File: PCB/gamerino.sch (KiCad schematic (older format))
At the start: 47 parts, among them J1 USB_B_Micro, J2 LT2, J3 RT2, P1 JOY1, P2 JOY2, P3 ICSP, P4 AUX, SW1 HATSWITCH, SW10 OPTS, SW11 X, SW12 B, SW13 A, SW14 Y, SW2 LT1, SW3 LT2, SW4 RT1, SW5 RT2, SW6 SEL, SW7 START, SW8 BACK, SW9 HOME, U1 MIC5219-3.3YM5, U2 ATmega32U4, U3 TCA9539, X1 16MHz

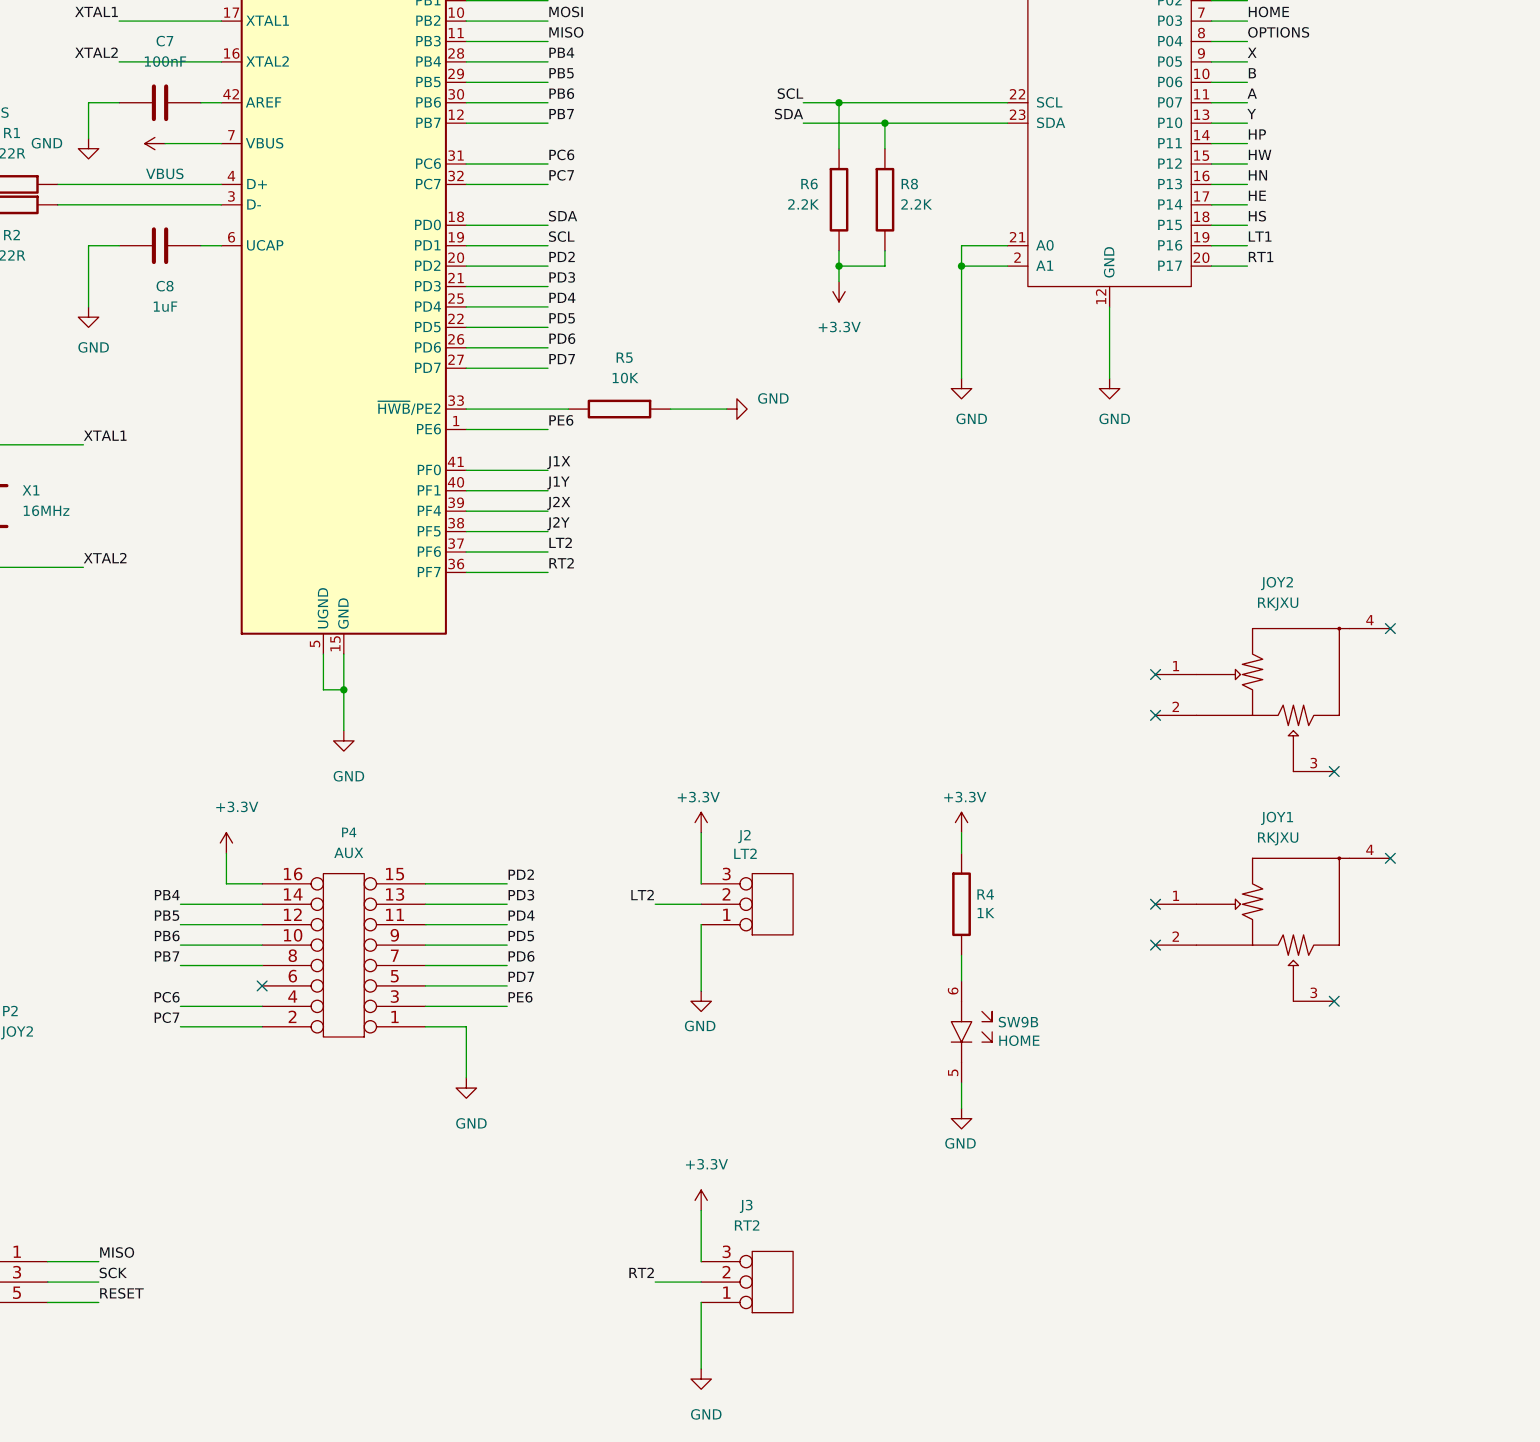
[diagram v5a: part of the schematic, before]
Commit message: Update schematics
Add LHOME net
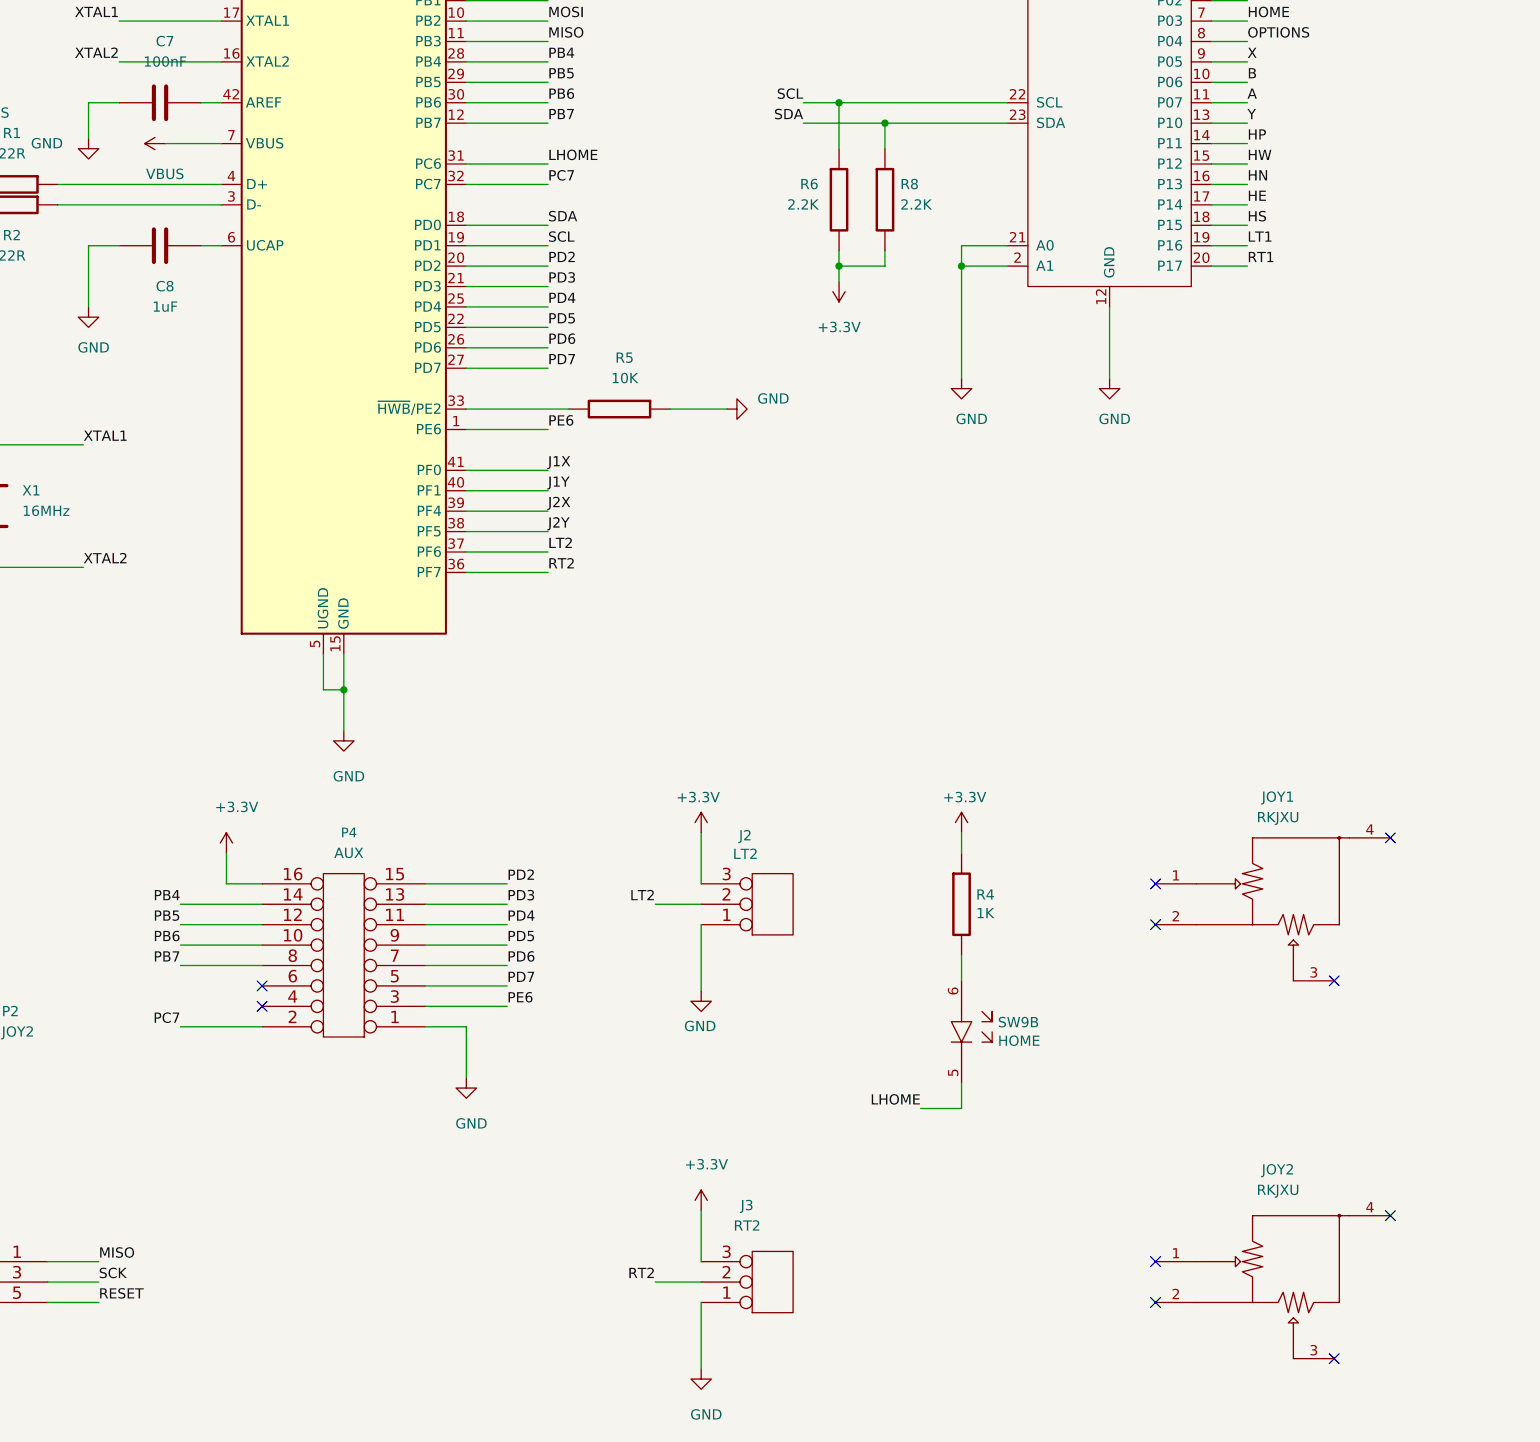
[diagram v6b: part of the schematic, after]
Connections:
- net GND: no longer SW9.5
- net PC6: no longer names the net of P4.4
- net PC6: no longer U2.31 (PC6)
- new net LHOME: SW9.5, U2.31 (PC6)
- no-connect marks 29 -> 30
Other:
- moved on the sheet: JOY1, JOY2
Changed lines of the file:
@@
 	6675 4450 7075 4450
 Text Label 7075 4450 0    50   ~ 0
-PC6
+LHOME
 Wire Wire Line
 	6675 4550 7075 4550
@@
 	1    0    0    -1
 $EndComp
-Wire Wire Line
-	5675 8575 5275 8575
-Text Label 5275 8575 2    50   ~ 0
-PC6
 Wire Wire Line
 	5675 8675 5275 8675
@@
 	9100 8950 9100 9075
 $Comp
-L gamerino-rescue:GND-power #PWR0102
-U 1 1 60BF772D
-P 9100 9075
-F 0 "#PWR0102" H 9100 8825 50  0001 C CNN
-F 1 "GND" H 9105 8902 50  0000 C CNN
-F 2 "" H 9100 9075 50  0001 C CNN
-F 3 "" H 9100 9075 50  0001 C CNN
-	1    9100 9075
-	-1   0    0    -1
-$EndComp
-$Comp
 L gamerino-rescue:+3.3V-power #PWR0103
 U 1 1 60C0ACCD
@@
 L gamerino:RKJXU JOY1
 U 1 1 60AED526
-P 10725 8075
-F 0 "JOY1" H 10650 8500 50  0000 C CNN
-F 1 "RKJXU" H 10650 8400 50  0000 C CNN
-F 2 "alps:RKJXU" H 10050 8075 50  0001 C CNN
-F 3 "" H 10050 8075 50  0001 C CNN
-F 4 "RKJXU1210006" H 10725 8075 50  0001 C CNN "MPN"
-F 5 "ALPS Alpine" H 10725 8075 50  0001 C CNN "Manufacturer"
-	1    10725 8075
+P 10725 7975
+F 0 "JOY1" H 10650 8400 50  0000 C CNN
+F 1 "RKJXU" H 10650 8300 50  0000 C CNN
+F 2 "alps:RKJXU" H 10050 7975 50  0001 C CNN
+F 3 "" H 10050 7975 50  0001 C CNN
+F 4 "RKJXU1210006" H 10725 7975 50  0001 C CNN "MPN"
+F 5 "ALPS Alpine" H 10725 7975 50  0001 C CNN "Manufacturer"
+	1    10725 7975
 	1    0    0    -1
 $EndComp
@@
 L gamerino:RKJXU JOY2
 U 1 1 60AF097E
-P 10725 6950
-F 0 "JOY2" H 10650 7400 50  0000 C CNN
-F 1 "RKJXU" H 10650 7300 50  0000 C CNN
-F 2 "alps:RKJXU" H 10050 6950 50  0001 C CNN
-F 3 "" H 10050 6950 50  0001 C CNN
-F 4 "RKJXU1210006" H 10725 6950 50  0001 C CNN "MPN"
-F 5 "ALPS Alpine" H 10725 6950 50  0001 C CNN "Manufacturer"
-	1    10725 6950
-	1    0    0    -1
-$EndComp
-NoConn ~ 10050 6950
-NoConn ~ 10050 7150
-NoConn ~ 10925 7425
-NoConn ~ 11200 6725
-NoConn ~ 11200 7850
-NoConn ~ 10050 8075
-NoConn ~ 10050 8275
-NoConn ~ 10925 8550
+P 10725 9825
+F 0 "JOY2" H 10650 10275 50  0000 C CNN
+F 1 "RKJXU" H 10650 10175 50  0000 C CNN
+F 2 "alps:RKJXU" H 10050 9825 50  0001 C CNN
+F 3 "" H 10050 9825 50  0001 C CNN
+F 4 "RKJXU1210006" H 10725 9825 50  0001 C CNN "MPN"
+F 5 "ALPS Alpine" H 10725 9825 50  0001 C CNN "Manufacturer"
+	1    10725 9825
+	1    0    0    -1
+$EndComp
+NoConn ~ 10050 9825
+NoConn ~ 10050 10025
+NoConn ~ 10925 10300
+NoConn ~ 11200 9600
+NoConn ~ 11200 7750
+NoConn ~ 10050 7975
+NoConn ~ 10050 8175
+NoConn ~ 10925 8450
+Wire Wire Line
+	9100 9075 8900 9075
+Text Label 8900 9075 2    50   ~ 0
+LHOME
+NoConn ~ 5675 8575
 $EndSCHEMATC

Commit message: Update Layout
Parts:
- J2, J3: footprint gamerino:53398-0371 -> gamerino:Molex_PicoBlade_53047-0310_1x03_P1.25mm_Vertical
- R1, R2: footprint Resistor_SMD:R_0603_1608Metric -> Resistor_SMD:R_0402_1005Metric; MPN RT0603FRE0722RL -> (none); Manufacturer Yageo -> (none)
- SW10, SW6, SW7, SW8: footprint gamerino:TL1105-T -> gamerino:TL6210; MPN TL1105TF160Q -> TL6210AF200GQ
- SW9: footprint gamerino:TL1220 -> gamerino:TL3265; MPN TL1220R3BBBNN -> TL3265GQSCLR
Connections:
- net D-: now reaches R2.1, U2.3 (D-)
- net D+: now reaches R1.1, U2.4 (D+)
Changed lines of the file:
@@
 F 0 "R1" V 4175 4575 50  0000 C CNN
 F 1 "22R" V 4275 4575 50  0000 C CNN
-F 2 "Resistor_SMD:R_0603_1608Metric" V 4355 4550 30  0001 C CNN
+F 2 "Resistor_SMD:R_0402_1005Metric" V 4355 4550 30  0001 C CNN
 F 3 "" H 4425 4550 30  0000 C CNN
-F 4 "RT0603FRE0722RL" H 4425 4550 50  0001 C CNN "MPN"
-F 5 "Yageo" H 4425 4550 50  0001 C CNN "Manufacturer"
+F 4 "" H 4425 4550 50  0001 C CNN "MPN"
+F 5 "" H 4425 4550 50  0001 C CNN "Manufacturer"
 	1    4425 4550
 	0    1    1    0
@@
 F 0 "R2" V 4575 4675 50  0000 C CNN
 F 1 "22R" V 4675 4675 50  0000 C CNN
-F 2 "Resistor_SMD:R_0603_1608Metric" V 4355 4650 30  0001 C CNN
+F 2 "Resistor_SMD:R_0402_1005Metric" V 4355 4650 30  0001 C CNN
 F 3 "" H 4425 4650 30  0000 C CNN
-F 4 "RT0603FRE0722RL" H 4425 4650 50  0001 C CNN "MPN"
-F 5 "Yageo" H 4425 4650 50  0001 C CNN "Manufacturer"
+F 4 "" H 4425 4650 50  0001 C CNN "MPN"
+F 5 "" H 4425 4650 50  0001 C CNN "Manufacturer"
 	1    4425 4650
 	0    1    1    0
@@
 F 0 "J3" H 8050 9550 50  0000 C CNN
 F 1 "RT2" H 8050 9650 50  0000 C CNN
-F 2 "gamerino:53398-0371" H 8175 9925 50  0001 C CNN
+F 2 "gamerino:Molex_PicoBlade_53047-0310_1x03_P1.25mm_Vertical" H 8175 9925 50  0001 C CNN
 F 3 "" H 8175 9925 50  0001 C CNN
 F 4 "53047-0310" H 8175 9925 50  0001 C CNN "MPN"
@@
 F 0 "J2" H 8042 7739 50  0000 C CNN
 F 1 "LT2" H 8042 7830 50  0000 C CNN
-F 2 "gamerino:53398-0371" H 8175 8075 50  0001 C CNN
+F 2 "gamerino:Molex_PicoBlade_53047-0310_1x03_P1.25mm_Vertical" H 8175 8075 50  0001 C CNN
 F 3 "" H 8175 8075 50  0001 C CNN
 F 4 "53047-0310" H 8175 8075 50  0001 C CNN "MPN"
@@
 F 0 "SW9" H 14467 3431 50  0000 C CNN
 F 1 "HOME" H 14467 3340 50  0000 C CNN
-F 2 "gamerino:TL1220" H 14450 3250 50  0001 C CNN
+F 2 "gamerino:TL3265" H 14450 3250 50  0001 C CNN
 F 3 "" H 14450 3250 50  0001 C CNN
-F 4 "TL1220R3BBBNN" H 14450 3100 50  0001 C CNN "MPN"
+F 4 "TL3265GQSCLR" H 14450 3100 50  0001 C CNN "MPN"
 F 5 "E-Switch" H 14450 3100 50  0001 C CNN "Manufacturer"
 	1    14450 3100
@@
 F 0 "SW9" V 8846 8222 50  0000 R CNN
 F 1 "HOME" V 8755 8222 50  0000 R CNN
-F 2 "gamerino:TL1220" H 8800 8850 50  0001 C CNN
+F 2 "gamerino:TL3265" H 8800 8850 50  0001 C CNN
 F 3 "" H 8800 8850 50  0001 C CNN
-F 4 "TL1220R3BBBNN" H 8800 8700 50  0001 C CNN "MPN"
+F 4 "TL3265GQSCLR" H 8800 8700 50  0001 C CNN "MPN"
 F 5 "E-Switch" H 8800 8700 50  0001 C CNN "Manufacturer"
 	2    8800 8700
@@
 F 0 "SW6" H 14467 1781 50  0000 C CNN
 F 1 "SEL" H 14467 1690 50  0000 C CNN
-F 2 "gamerino:TL1105-T" H 14450 1100 50  0001 C CNN
+F 2 "gamerino:TL6210" H 14450 1100 50  0001 C CNN
 F 3 "" H 14450 1100 50  0001 C CNN
-F 4 "TL1105TF160Q" H 14450 1450 50  0001 C CNN "MPN"
+F 4 "TL6210AF200GQ" H 14450 1450 50  0001 C CNN "MPN"
 F 5 "E-Switch" H 14450 1450 50  0001 C CNN "Manufacturer"
 	1    14450 1450
@@
 F 0 "SW7" H 14467 2306 50  0000 C CNN
 F 1 "START" H 14467 2215 50  0000 C CNN
-F 2 "gamerino:TL1105-T" H 14450 1625 50  0001 C CNN
+F 2 "gamerino:TL6210" H 14450 1625 50  0001 C CNN
 F 3 "" H 14450 1625 50  0001 C CNN
-F 4 "TL1105TF160Q" H 14450 1975 50  0001 C CNN "MPN"
+F 4 "TL6210AF200GQ" H 14450 1975 50  0001 C CNN "MPN"
 F 5 "E-Switch" H 14450 1975 50  0001 C CNN "Manufacturer"
 	1    14450 1975
@@
 F 0 "SW8" H 14467 2856 50  0000 C CNN
 F 1 "BACK" H 14467 2765 50  0000 C CNN
-F 2 "gamerino:TL1105-T" H 14450 2175 50  0001 C CNN
+F 2 "gamerino:TL6210" H 14450 2175 50  0001 C CNN
 F 3 "" H 14450 2175 50  0001 C CNN
-F 4 "TL1105TF160Q" H 14450 2525 50  0001 C CNN "MPN"
+F 4 "TL6210AF200GQ" H 14450 2525 50  0001 C CNN "MPN"
 F 5 "E-Switch" H 14450 2525 50  0001 C CNN "Manufacturer"
 	1    14450 2525
@@
 F 0 "SW10" H 14467 3981 50  0000 C CNN
 F 1 "OPTS" H 14467 3890 50  0000 C CNN
-F 2 "gamerino:TL1105-T" H 14450 3800 50  0001 C CNN
+F 2 "gamerino:TL6210" H 14450 3800 50  0001 C CNN
 F 3 "" H 14450 3800 50  0001 C CNN
-F 4 "TL1105TF160Q" H 14450 3650 50  0001 C CNN "MPN"
+F 4 "TL6210AF200GQ" H 14450 3650 50  0001 C CNN "MPN"
 F 5 "E-Switch" H 14450 3650 50  0001 C CNN "Manufacturer"
 	1    14450 3650
@@
 LHOME
 NoConn ~ 5675 8575
+Text Label 4725 4550 0    50   ~ 0
+D+
+Text Label 4725 4650 0    50   ~ 0
+D-
 $EndSCHEMATC

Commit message: Update BOM
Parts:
- C10, C6, C7: MPN (none) -> 885012206020; Manufacturer (none) -> Wurth
- C3, C4: MPN (none) -> CGA2B2C0G1H180J050BA; Manufacturer (none) -> TDK
- C5, C8, C9: MPN (none) -> CGA3E1X7R1C105K080AC; Manufacturer (none) -> TDK
- P3: MPN (none) -> MTLW-103-07-G-S-230; Manufacturer (none) -> Samtec
- P4: MPN (none) -> CLM-108-02-F-D; Manufacturer (none) -> Samtec
- R1, R2: MPN (none) -> CRCW040222R0FKED; Manufacturer (none) -> Vishay
- R3, R5, R7: MPN (none) -> RC0603FR-0710KL; Manufacturer (none) -> Yageo
- R4: MPN (none) -> CRG0603F1K0; Manufacturer (none) -> TE
- R6, R8, R9: MPN (none) -> MCR03EZPFX2201; Manufacturer (none) -> ROHM
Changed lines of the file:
@@
 F 2 "Resistor_SMD:R_0603_1608Metric" V 8655 3550 30  0001 C CNN
 F 3 "" H 8725 3550 30  0000 C CNN
+F 4 "RC0603FR-0710KL" H 8725 3550 50  0001 C CNN "MPN"
+F 5 "Yageo" H 8725 3550 50  0001 C CNN "Manufacturer"
 	1    8725 3550
 	0    1    1    0
@@
 F 2 "Capacitor_SMD:C_0402_1005Metric" H 4013 6275 30  0001 C CNN
 F 3 "" H 3975 6425 60  0000 C CNN
+F 4 "CGA2B2C0G1H180J050BA" H 3975 6425 50  0001 C CNN "MPN"
+F 5 "TDK" H 3975 6425 50  0001 C CNN "Manufacturer"
 	1    3975 6425
 	0    1    1    0
@@
 F 2 "Capacitor_SMD:C_0402_1005Metric" H 4013 5675 30  0001 C CNN
 F 3 "" H 3975 5825 60  0000 C CNN
+F 4 "CGA2B2C0G1H180J050BA" H 3975 5825 50  0001 C CNN "MPN"
+F 5 "TDK" H 3975 5825 50  0001 C CNN "Manufacturer"
 	1    3975 5825
 	0    1    1    0
@@
 F 2 "Connector_PinHeader_2.54mm:PinHeader_2x03_P2.54mm_Vertical" H 4225 9975 50  0001 C CNN
 F 3 "" H 4225 9975 50  0001 C CNN
+F 4 "MTLW-103-07-G-S-230" H 4225 9975 50  0001 C CNN "MPN"
+F 5 "Samtec" H 4225 9975 50  0001 C CNN "Manufacturer"
 	1    4225 9975
 	-1   0    0    -1
@@
 F 2 "Capacitor_SMD:C_0603_1608Metric" H 10263 2950 30  0001 C CNN
 F 3 "" H 10225 3100 60  0000 C CNN
+F 4 "885012206020" H 10225 3100 50  0001 C CNN "MPN"
+F 5 "Wurth" H 10225 3100 50  0001 C CNN "Manufacturer"
 	1    10225 3100
 	0    1    1    0
@@
 F 2 "Capacitor_SMD:C_0603_1608Metric" H 5213 4700 30  0001 C CNN
 F 3 "" H 5175 4850 60  0000 C CNN
+F 4 "CGA3E1X7R1C105K080AC" H 5175 4850 50  0001 C CNN "MPN"
+F 5 "TDK" H 5175 4850 50  0001 C CNN "Manufacturer"
 	1    5175 4850
 	0    -1   -1   0
@@
 F 2 "Capacitor_SMD:C_0603_1608Metric" H 5213 4000 30  0001 C CNN
 F 3 "" H 5175 4150 60  0000 C CNN
+F 4 "885012206020" H 5175 4150 50  0001 C CNN "MPN"
+F 5 "Wurth" H 5175 4150 50  0001 C CNN "Manufacturer"
 	1    5175 4150
 	0    -1   -1   0
@@
 F 2 "Capacitor_SMD:C_0603_1608Metric" H 4088 1750 30  0001 C CNN
 F 3 "" H 4050 1900 60  0000 C CNN
+F 4 "CGA3E1X7R1C105K080AC" H 4050 1900 50  0001 C CNN "MPN"
+F 5 "TDK" H 4050 1900 50  0001 C CNN "Manufacturer"
 	1    4050 1900
 	-1   0    0    -1
@@
 F 2 "Resistor_SMD:R_0603_1608Metric" V 8430 4625 30  0001 C CNN
 F 3 "" H 8500 4625 30  0000 C CNN
+F 4 "MCR03EZPFX2201" H 8500 4625 50  0001 C CNN "MPN"
+F 5 "ROHM" H 8500 4625 50  0001 C CNN "Manufacturer"
 	1    8500 4625
 	1    0    0    -1
@@
 F 2 "Resistor_SMD:R_0603_1608Metric" V 8655 4625 30  0001 C CNN
 F 3 "" H 8725 4625 30  0000 C CNN
+F 4 "MCR03EZPFX2201" H 8725 4625 50  0001 C CNN "MPN"
+F 5 "ROHM" H 8725 4625 50  0001 C CNN "Manufacturer"
 	1    8725 4625
 	1    0    0    -1
@@
 F 2 "Resistor_SMD:R_0603_1608Metric" V 9155 3050 30  0001 C CNN
 F 3 "" H 9225 3050 30  0000 C CNN
+F 4 "MCR03EZPFX2201" H 9225 3050 50  0001 C CNN "MPN"
+F 5 "ROHM" H 9225 3050 50  0001 C CNN "Manufacturer"
 	1    9225 3050
 	1    0    0    -1
@@
 F 2 "Resistor_SMD:R_0402_1005Metric" V 4355 4550 30  0001 C CNN
 F 3 "" H 4425 4550 30  0000 C CNN
-F 4 "" H 4425 4550 50  0001 C CNN "MPN"
-F 5 "" H 4425 4550 50  0001 C CNN "Manufacturer"
+F 4 "CRCW040222R0FKED" H 4425 4550 50  0001 C CNN "MPN"
+F 5 "Vishay" H 4425 4550 50  0001 C CNN "Manufacturer"
 	1    4425 4550
 	0    1    1    0
@@
 F 2 "Resistor_SMD:R_0402_1005Metric" V 4355 4650 30  0001 C CNN
 F 3 "" H 4425 4650 30  0000 C CNN
-F 4 "" H 4425 4650 50  0001 C CNN "MPN"
-F 5 "" H 4425 4650 50  0001 C CNN "Manufacturer"
+F 4 "CRCW040222R0FKED" H 4425 4650 50  0001 C CNN "MPN"
+F 5 "Vishay" H 4425 4650 50  0001 C CNN "Manufacturer"
 	1    4425 4650
 	0    1    1    0
@@
 F 2 "Capacitor_SMD:C_0603_1608Metric" H 5513 2975 30  0001 C CNN
 F 3 "" H 5475 3125 60  0001 C CNN
+F 4 "CGA3E1X7R1C105K080AC" H 5475 3125 50  0001 C CNN "MPN"
+F 5 "TDK" H 5475 3125 50  0001 C CNN "Manufacturer"
 	1    5475 3125
 	0    1    1    0
@@
 F 2 "Capacitor_SMD:C_0603_1608Metric" H 4588 1750 30  0001 C CNN
 F 3 "" H 4550 1900 60  0000 C CNN
+F 4 "885012206020" H 4550 1900 50  0001 C CNN "MPN"
+F 5 "Wurth" H 4550 1900 50  0001 C CNN "Manufacturer"
 	1    4550 1900
 	-1   0    0    -1
@@
 F 2 "Resistor_SMD:R_0603_1608Metric" V 9030 8075 30  0001 C CNN
 F 3 "" H 9100 8075 30  0000 C CNN
+F 4 "CRG0603F1K0" H 9100 8075 50  0001 C CNN "MPN"
+F 5 "TE" H 9100 8075 50  0001 C CNN "Manufacturer"
 	1    9100 8075
 	1    0    0    -1
@@
 F 2 "Resistor_SMD:R_0603_1608Metric" V 4480 3050 30  0001 C CNN
 F 3 "" H 4550 3050 30  0000 C CNN
+F 4 "RC0603FR-0710KL" H 4550 3050 50  0001 C CNN "MPN"
+F 5 "Yageo" H 4550 3050 50  0001 C CNN "Manufacturer"
 	1    4550 3050
 	-1   0    0    1
@@
 F 2 "Connector_PinSocket_1.00mm:PinSocket_2x08_P1.00mm_Vertical_SMD" H 6075 8325 50  0001 C CNN
 F 3 "" H 6075 8325 50  0001 C CNN
+F 4 "CLM-108-02-F-D" H 6075 8325 50  0001 C CNN "MPN"
+F 5 "Samtec" H 6075 8325 50  0001 C CNN "Manufacturer"
 	1    6075 8325
 	-1   0    0    1
@@
 F 2 "Resistor_SMD:R_0603_1608Metric" V 7275 5675 30  0001 C CNN
 F 3 "" H 7425 5650 30  0000 C CNN
+F 4 "RC0603FR-0710KL" H 7425 5650 50  0001 C CNN "MPN"
+F 5 "Yageo" H 7425 5650 50  0001 C CNN "Manufacturer"
 	1    7425 5650
 	0    1    1    0
